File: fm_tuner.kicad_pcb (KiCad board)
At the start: 2 copper layers, 90.4 x 68.6 mm, 17 parts, among them IC1 ATMEGA328P-A, J1 ISP_Header, P2 USB_B, SW1 SW_PUSH, U1 16x2_LCD, U2 si4713_module

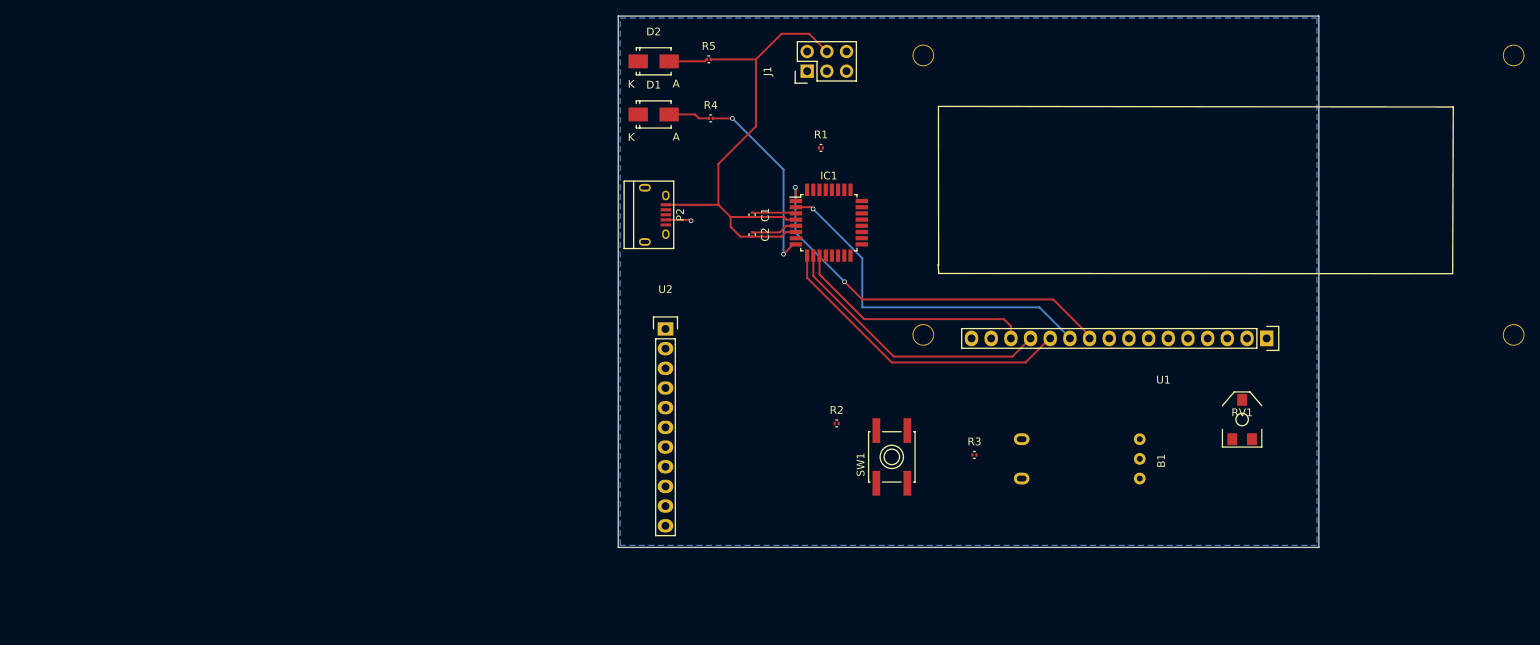
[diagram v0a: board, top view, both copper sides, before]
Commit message: added first pass of routes to the board
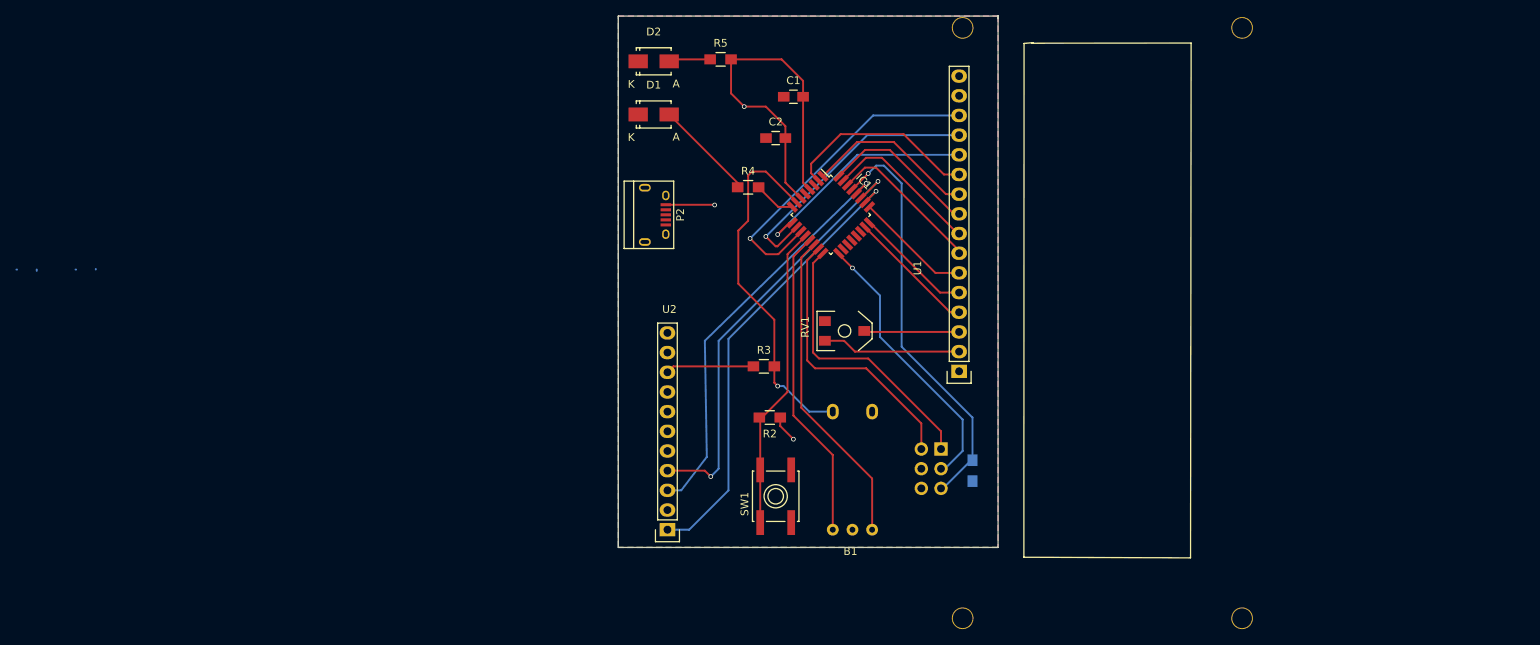
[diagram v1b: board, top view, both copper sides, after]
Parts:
- C1, C2: footprint Capacitors_SMD:C_0201 -> Capacitors_SMD:C_0805_HandSoldering
- J1: moved to B.Cu
- R1: footprint Resistors_SMD:R_0201 -> Resistors_SMD:R_0805_HandSoldering; moved to B.Cu
- R2, R3, R4, R5: footprint Resistors_SMD:R_0201 -> Resistors_SMD:R_0805_HandSoldering
- moved U1 80.0 mm to (57.7, 90.9), turned to 90 degrees
- moved RV1 52.6 mm to (42.4, 53.8), turned to 270 degrees
- moved J1 51.7 mm to (54.9, 69.1), turned to 180 degrees
- moved R1 46.0 mm to (58.9, 71.9), turned to 90 degrees
- moved R3 29.5 mm to (32.0, 58.4)
- moved U2 25.9 mm to (19.6, 79.5), turned to 180 degrees
- moved B1 25.9 mm to (40.9, 64.3), turned to 0 degrees
- moved C1 16.1 mm to (35.8, 23.6), turned to 0 degrees
- moved SW1 15.8 mm to (33.5, 75.2)
- moved C2 12.8 mm to (33.5, 29.0), turned to 0 degrees
- moved R4 10.1 mm to (30.0, 35.3)
- moved R2 8.67 mm to (32.8, 65.0), turned to 180 degrees
- moved R5 1.52 mm to (26.4, 18.8)
- moved IC1 1.05 mm to (40.6, 38.9), turned to 315 degrees
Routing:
- net Net-(IC1-Pad26): track 0.00 -> 58.6 mm, vias 0 -> 1
- net Net-(IC1-Pad27): track 0.00 -> 56.2 mm, vias 0 -> 2
- net Net-(IC1-Pad29): track 0.00 -> 54.4 mm, vias 0 -> 1
- net Net-(IC1-Pad28): track 0.00 -> 53.2 mm, vias 0 -> 1
- net /set: track 0.00 -> 46.4 mm, vias 0 -> 1
- net /B: track 0.00 -> 41.3 mm
- net /A: track 0.00 -> 40.3 mm
- net /a-tune: track 0.00 -> 39.7 mm
- net Net-(IC1-Pad15): track 0.00 -> 36.4 mm
- net Net-(IC1-Pad16): track 0.00 -> 36.3 mm
- net Net-(IC1-Pad17): track 0.00 -> 35.9 mm, vias 0 -> 1
- net Net-(IC1-Pad1): track 51.5 -> 22.2 mm, vias 2 -> 0
- net VCC: track 66.1 -> 87.5 mm, vias 0 -> 3
- net Net-(IC1-Pad2): track 46.1 -> 25.4 mm, vias 1 -> 0
- net Net-(IC1-Pad32): track 0.08 -> 20.4 mm
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- added copper zone on F.Cu, net GND
- added copper zone on B.Cu, net VCC
- removed copper zone on B.Cu, net GND
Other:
- board size 90.4 x 68.6 mm -> 49 x 68.6 mm

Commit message: finished routing? added text description to board. created fabrication outputs(gerber and drill files)
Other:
- board text added: "Designed by: Max Redmond Electromancy"
- board text added: "FM tuner v.1"
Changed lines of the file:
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@@
     (links 57)
     (no_connects 6)
-    (area 13.132999 13.132999 103.707001 81.863001)
+    (area -64.790201 13.132999 95.323 92.529)
     (thickness 1.6)
-    (drawings 6)
+    (drawings 8)
     (tracks 174)
     (zones 0)
@@
     (visible_elements FFFFF77F)
     (pcbplotparams
-      (layerselection 0x00030_80000001)
+      (layerselection 0x010f0_80000001)
       (usegerberextensions false)
       (excludeedgelayer true)
@@
       (outputformat 1)
       (mirror false)
-      (drillshape 1)
+      (drillshape 0)
       (scaleselection 1)
-      (outputdirectory ""))
+      (outputdirectory fabrication/))
   )
   (net 0 "")
@@
     (descr "Through hole pin header")
     (tags "pin header")
-    (fp_text reference J1 (at 0 5.1 180) (layer B.SilkS)
+    (fp_text reference J1 (at 0.762 -8.128 180) (layer B.SilkS)
       (effects (font (size 1 1) (thickness 0.15)) (justify mirror))
     )
-    (fp_text value ISP_Header (at 0 3.1 180) (layer B.Fab)
+    (fp_text value ISP_Header (at 0 3.1 180) (layer B.Fab) hide
       (effects (font (size 1 1) (thickness 0.15)) (justify mirror))
     )
@@
       (effects (font (size 1 1) (thickness 0.15)))
     )
-    (fp_text value SW_PUSH (at 0 0 90) (layer F.Fab)
+    (fp_text value SW_PUSH (at 0 0 90) (layer F.Fab) hide
       (effects (font (size 1 1) (thickness 0.15)))
     )
@@
     (tags "QFP 0.8")
     (attr smd)
-    (fp_text reference IC1 (at 0 -6.05 315) (layer F.SilkS)
-      (effects (font (size 1 1) (thickness 0.15)))
-    )
-    (fp_text value ATMEGA328P-A (at 0 6.05 315) (layer F.Fab)
+    (fp_text reference IC1 (at 0 -6.05 315) (layer F.SilkS) hide
+      (effects (font (size 1 1) (thickness 0.15)))
+    )
+    (fp_text value ATMEGA328P-A (at 0 6.05 315) (layer F.Fab) hide
       (effects (font (size 1 1) (thickness 0.15)))
     )
@@
     (tags "CMS POT")
     (attr smd)
-    (fp_text reference RV1 (at -0.508 5.08 270) (layer F.SilkS)
-      (effects (font (size 1 1) (thickness 0.15)))
-    )
-    (fp_text value POT (at -0.508 -5.08 450) (layer F.Fab)
+    (fp_text reference RV1 (at -3.81 0.762 360) (layer F.SilkS)
+      (effects (font (size 1 1) (thickness 0.15)))
+    )
+    (fp_text value POT (at -0.508 -5.08 270) (layer F.Fab) hide
       (effects (font (size 1 1) (thickness 0.15)))
     )
@@
     (descr "16x2 LCD footprint qith 16 pins")
     (tags "pin header")
-    (fp_text reference U1 (at 45.212 -5.8166 90) (layer F.SilkS)
-      (effects (font (size 1 1) (thickness 0.15)))
-    )
-    (fp_text value 16x2_LCD (at 31.877 -5.6896 90) (layer F.Fab)
+    (fp_text reference U1 (at 28.448 1.016 90) (layer F.SilkS)
+      (effects (font (size 1 1) (thickness 0.15)))
+    )
+    (fp_text value 16x2_LCD (at 31.877 -5.6896 90) (layer F.Fab) hide
       (effects (font (size 1 1) (thickness 0.15)))
     )
@@
       (effects (font (size 1 1) (thickness 0.15)))
     )
-    (fp_text value si4713_module (at -1.27 30.48 180) (layer F.Fab)
+    (fp_text value si4713_module (at -1.27 30.48 180) (layer F.Fab) hide
       (effects (font (size 1 1) (thickness 0.15)))
     )
@@
       (effects (font (size 1 1) (thickness 0.15)))
     )
-    (fp_text value USB_B (at 0 4.8 270) (layer F.Fab)
+    (fp_text value USB_B (at 3.81 -3.556 270) (layer F.Fab)
       (effects (font (size 1 1) (thickness 0.15)))
     )
@@
   (module fm_tuner:rotary_encoder (layer F.Cu)
     (at 40.894 64.262)
-    (fp_text reference B1 (at 2.286 18.034) (layer F.SilkS)
-      (effects (font (size 1 1) (thickness 0.15)))
-    )
-    (fp_text value Rotary_encoder (at 5.4356 -2.6162) (layer F.Fab)
+    (fp_text reference B1 (at 3.556 3.556) (layer F.SilkS)
+      (effects (font (size 1 1) (thickness 0.15)))
+    )
+    (fp_text value Rotary_encoder (at 2.286 -2.794) (layer F.Fab) hide
       (effects (font (size 1 1) (thickness 0.15)))
     )
@@
       (effects (font (size 1 1) (thickness 0.15)))
     )
-    (fp_text value Led_Small (at 0 4.3) (layer F.Fab)
+    (fp_text value Led_Small (at 0 4.3) (layer F.Fab) hide
       (effects (font (size 1 1) (thickness 0.15)))
     )
@@
       (effects (font (size 1 1) (thickness 0.15)))
     )
-    (fp_text value Led_Small (at 0 4.3) (layer F.Fab)
+    (fp_text value Led_Small (at 0 4.3) (layer F.Fab) hide
       (effects (font (size 1 1) (thickness 0.15)))
     )
@@
       (effects (font (size 1 1) (thickness 0.15)))
     )
-    (fp_text value 100n (at 0 2.1) (layer F.Fab)
+    (fp_text value 100n (at 3.302 -1.778) (layer F.Fab)
       (effects (font (size 1 1) (thickness 0.15)))
     )
@@
     (tags "capacitor 0805")
     (attr smd)
-    (fp_text reference C2 (at 0 -2.1) (layer F.SilkS)
+    (fp_text reference C2 (at -1.778 -1.778) (layer F.SilkS)
       (effects (font (size 1 1) (thickness 0.15)))
     )
@@
       (effects (font (size 1 1) (thickness 0.15)))
     )
-    (fp_text value 10K (at 0 2.1 180) (layer F.Fab)
+    (fp_text value 10K (at 1.778 2.032 180) (layer F.Fab)
       (effects (font (size 1 1) (thickness 0.15)))
     )
@@
       (effects (font (size 1 1) (thickness 0.15)))
     )
-    (fp_text value 10K (at 0 2.1) (layer F.Fab)
+    (fp_text value 10K (at -1.016 1.778) (layer F.Fab)
       (effects (font (size 1 1) (thickness 0.15)))
     )
@@
       (effects (font (size 1 1) (thickness 0.15)))
     )
-    (fp_text value R (at 0 2.1) (layer F.Fab)
+    (fp_text value R (at 0 2.1) (layer F.Fab) hide
       (effects (font (size 1 1) (thickness 0.15)))
     )
@@
       (effects (font (size 1 1) (thickness 0.15)))
     )
-    (fp_text value R (at 0 2.1) (layer F.Fab)
+    (fp_text value R (at 0 2.1) (layer F.Fab) hide
       (effects (font (size 1 1) (thickness 0.15)))
     )
@@
     )
   )
+  (gr_text "Designed by:\nMax Redmond\nElectromancy" (at 30.988 20.066) (layer B.Mask)
+    (effects (font (size 1.5 1.5) (thickness 0.3)) (justify left mirror))
+  )
+  (gr_text "FM tuner\nv.1\n" (at 37.338 16.51) (layer F.SilkS)
+    (effects (font (size 1.5 1.5) (thickness 0.3)) (justify left))
+  )
   (gr_line (start 62.23 13.462) (end 62.23 13.208) (angle 90) (layer Edge.Cuts) (width 0.15))
